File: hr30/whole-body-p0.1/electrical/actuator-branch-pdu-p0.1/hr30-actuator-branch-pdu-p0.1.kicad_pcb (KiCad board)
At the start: 6 copper layers, 82 x 42 mm, 78 parts, among them J1 12 V CONTROLLED INPUT, J101 CHANNEL 1 OUTPUT, J102 CHANNEL 2 OUTPUT, J103 CHANNEL 3 OUTPUT, J104 CHANNEL 4 OUTPUT, J105 CHANNEL 5 OUTPUT, J106 CHANNEL 6 OUTPUT, J2 6x DISABLE_OD + 6x PG, U201 TPS259474LRPWR circuit-breake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, U202 TPS259474LRPWR circuit-breake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, U203 TPS259474LRPWR circuit-breake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, U204 TPS259474LRPWR circuit-breake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, U205 TPS259474LRPWR circuit-breake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, U206 TPS259474LRPWR circuit-breake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

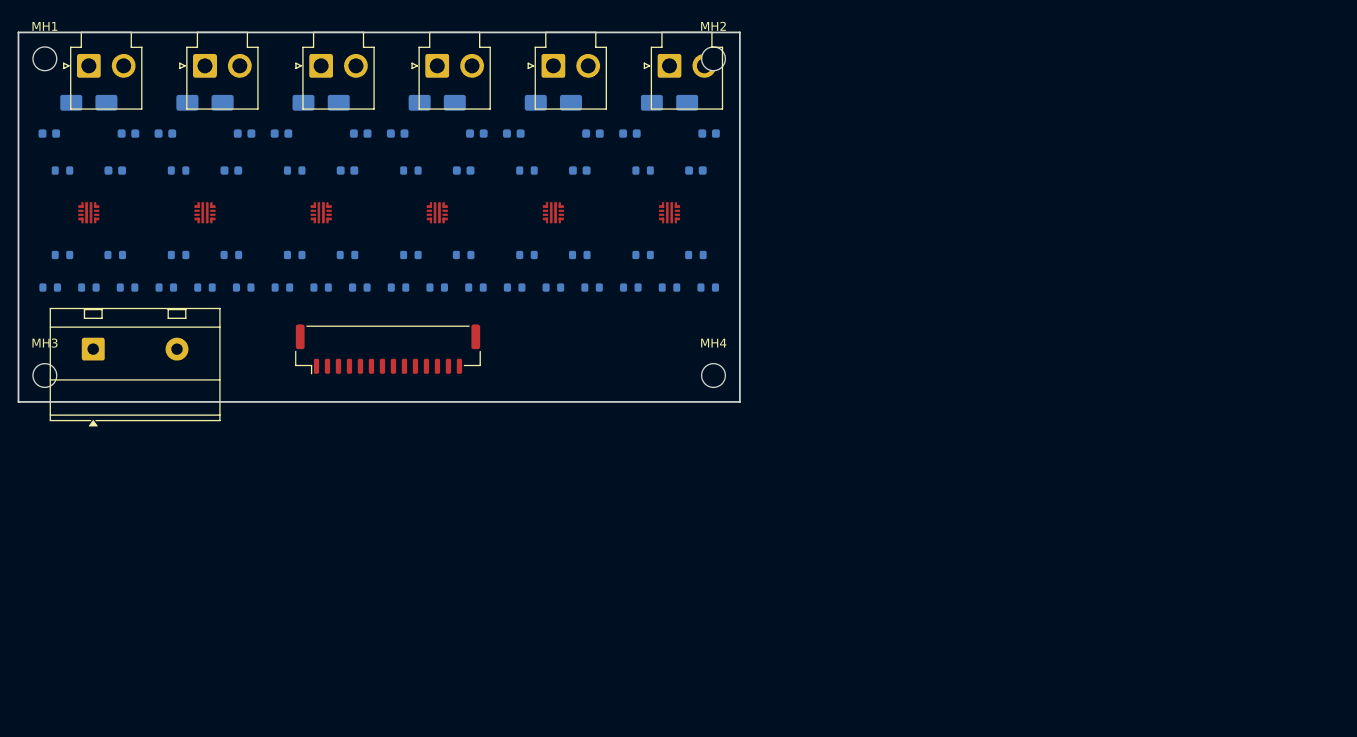
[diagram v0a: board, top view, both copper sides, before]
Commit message: Route HR-30 actuator branch PDU
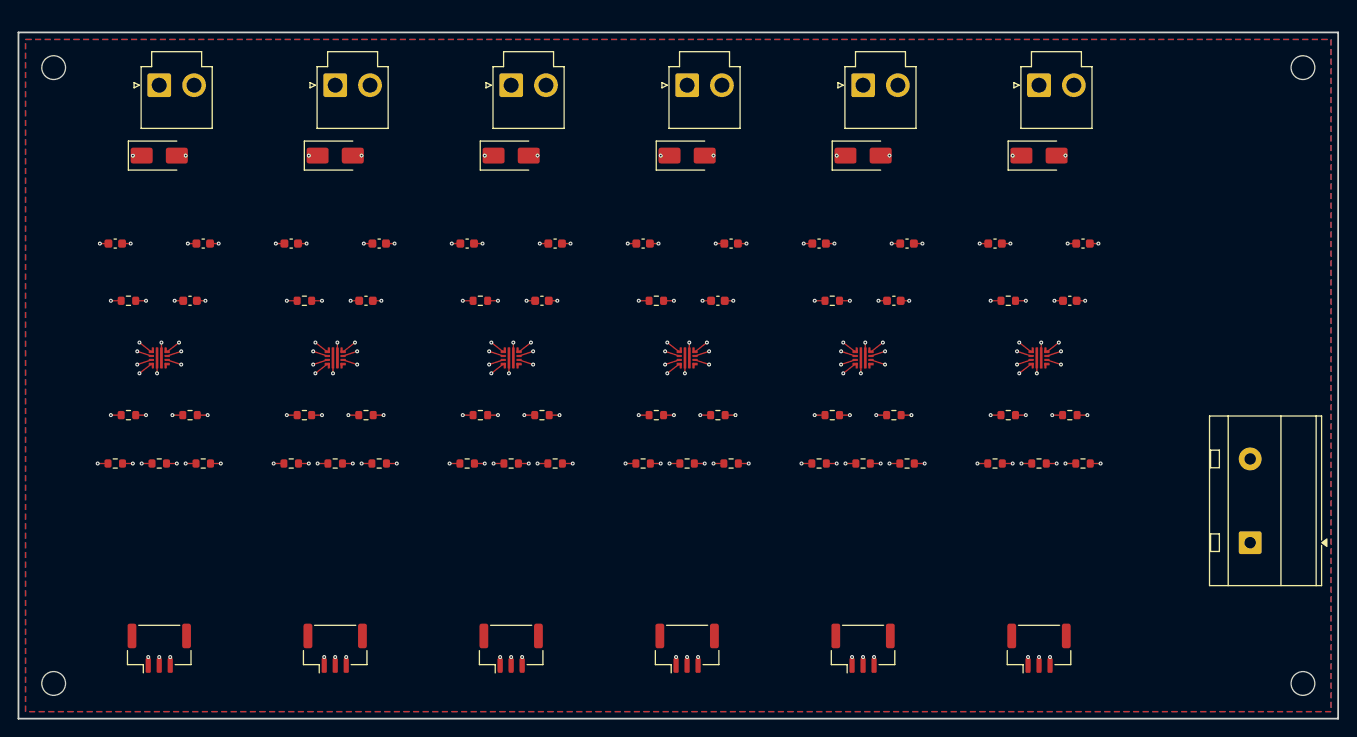
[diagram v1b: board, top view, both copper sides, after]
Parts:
- removed J2: 6x DISABLE_OD + 6x PG, JST_GH_BM14B-GHS-TBT_1x14-1MP_P1.25mm_Vertical
- added J201: CHANNEL 1 CONTROL, JST_GH_BM03B-GHS-TBT_1x03-1MP_P1.25mm_Vertical, F.Cu at (16.0, 70.0)
- added J202: CHANNEL 2 CONTROL, JST_GH_BM03B-GHS-TBT_1x03-1MP_P1.25mm_Vertical, F.Cu at (36.0, 70.0)
- added J203: CHANNEL 3 CONTROL, JST_GH_BM03B-GHS-TBT_1x03-1MP_P1.25mm_Vertical, F.Cu at (56.0, 70.0)
- added J204: CHANNEL 4 CONTROL, JST_GH_BM03B-GHS-TBT_1x03-1MP_P1.25mm_Vertical, F.Cu at (76.0, 70.0)
- added J205: CHANNEL 5 CONTROL, JST_GH_BM03B-GHS-TBT_1x03-1MP_P1.25mm_Vertical, F.Cu at (96.0, 70.0)
- added J206: CHANNEL 6 CONTROL, JST_GH_BM03B-GHS-TBT_1x03-1MP_P1.25mm_Vertical, F.Cu at (116.0, 70.0)
- C101, C102, C103, C201, C202, C203, C301, C302, C303, C401, C402, C403, C501, C502, C503, C601, C602, C603, D101, D201, D301, D401, D501, D601, R101, R102, R103, R104, R105, R106, R201, R202, R203, R204, R205, R206, R301, R302, R303, R304, R305, R306, R401, R402, R403, R404, R405, R406, R501, R502, R503, R504, R505, R506, R601, R602, R603, R604, R605, R606: moved to F.Cu
- moved J1 133.3 mm to (140.0, 58.0), turned to 90 degrees
- moved MH4 75.6 mm to (146.0, 74.0)
- moved MH2 67.0 mm to (146.0, 4.00)
- moved R603 47.1 mm to (121.0, 49.0), turned to 0 degrees
- moved R602 46.5 mm to (116.0, 49.0), turned to 0 degrees
- moved R605 46.2 mm to (119.5, 43.5), turned to 0 degrees
- moved R601 46.0 mm to (111.0, 49.0), turned to 0 degrees
- moved R604 45.3 mm to (112.5, 43.5), turned to 0 degrees
- moved U206 45.1 mm to (116.0, 37.0)
- moved C603 45.0 mm to (119.5, 30.5), turned to 0 degrees
- moved C602 44.3 mm to (121.0, 24.0), turned to 0 degrees
- moved R606 44.1 mm to (112.5, 30.5), turned to 0 degrees
- moved C601 43.3 mm to (111.0, 24.0), turned to 0 degrees
- moved D601 42.4 mm to (116.0, 14.0), turned to 0 degrees
- moved J106 42.1 mm to (116.0, 6.00)
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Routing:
- net PDU_12V_IN: track 0.00 -> 351.9 mm, vias 0 -> 18
- net PDU_0V: track 0.00 -> 60.5 mm, vias 0 -> 54
- net BRANCH_6_12V: track 0.00 -> 53.4 mm, vias 0 -> 4
- net BRANCH_5_12V: track 0.00 -> 53.4 mm, vias 0 -> 4
- net BRANCH_4_12V: track 0.00 -> 53.4 mm, vias 0 -> 4
- net BRANCH_3_12V: track 0.00 -> 53.4 mm, vias 0 -> 4
- net BRANCH_2_12V: track 0.00 -> 53.4 mm, vias 0 -> 4
- net BRANCH_1_12V: track 0.00 -> 53.4 mm, vias 0 -> 4
- net CH3_PG: track 0.00 -> 41.1 mm, vias 0 -> 2
- net CH2_PG: track 0.00 -> 41.1 mm, vias 0 -> 2
- net CH1_PG: track 0.00 -> 41.1 mm, vias 0 -> 2
- net CH6_PG: track 0.00 -> 41.1 mm, vias 0 -> 2
- net CH5_PG: track 0.00 -> 41.1 mm, vias 0 -> 2
- net CH4_PG: track 0.00 -> 41.1 mm, vias 0 -> 2
- net CH3_EN: track 0.00 -> 40.3 mm, vias 0 -> 4
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- added copper zone on B.Cu, net PDU_0V
- added copper zone on F.Cu, net PDU_0V
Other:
- board size 82 x 42 mm -> 150 x 78 mm
- copper layers 6 -> 10

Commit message: Install distributed HR-30 actuator power architecture
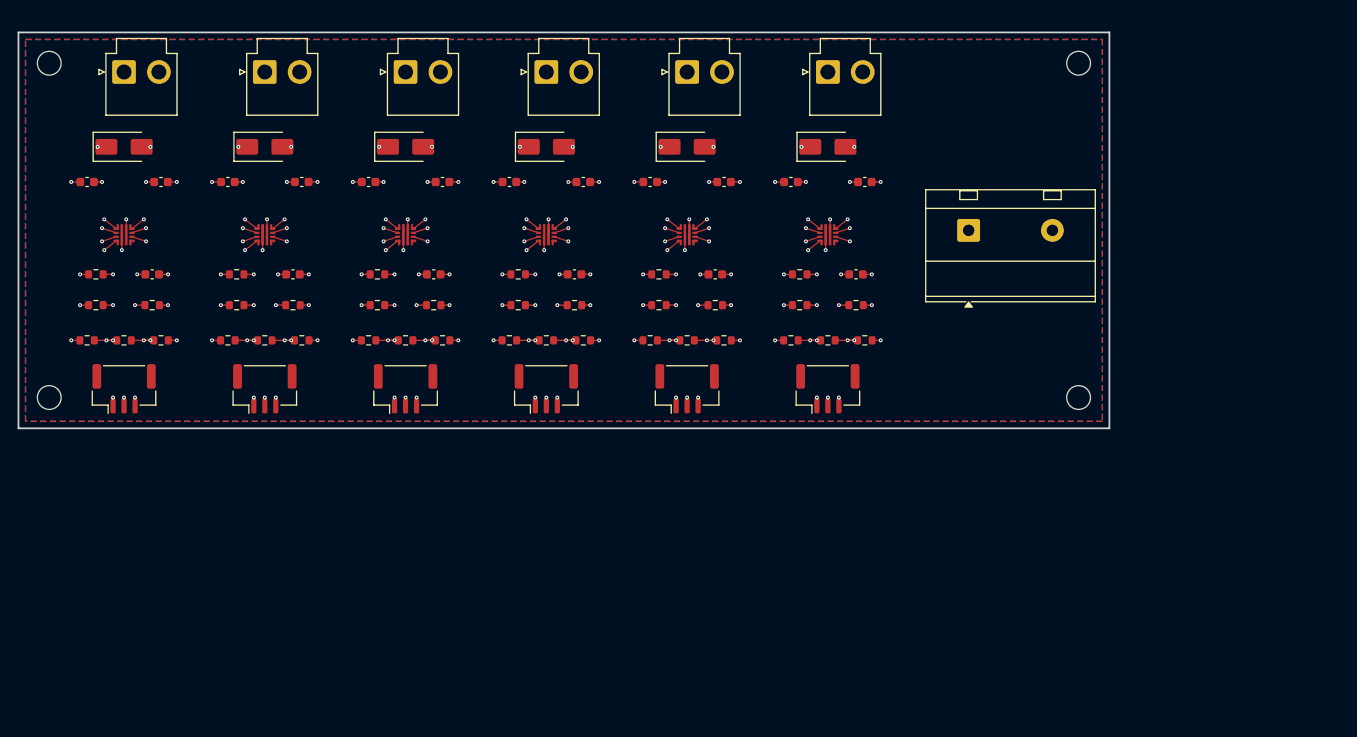
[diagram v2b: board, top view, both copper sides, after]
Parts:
- moved J1 47.8 mm to (108.0, 22.5), turned to 0 degrees
- moved MH4 41.3 mm to (120.5, 41.5)
- moved J206 38.0 mm to (92.0, 40.5)
- moved J205 35.6 mm to (76.0, 40.5)
- moved J204 33.6 mm to (60.0, 40.5)
- moved MH3 32.5 mm to (3.50, 41.5)
- moved J203 31.8 mm to (44.0, 40.5)
- moved J202 30.6 mm to (28.0, 40.5)
- moved J201 29.8 mm to (12.0, 40.5)
- moved R603 28.5 mm to (96.2, 35.0)
- moved R602 27.8 mm to (92.0, 35.0)
- moved U206 27.8 mm to (92.0, 23.0)
- moved R605 27.3 mm to (95.2, 31.0)
- moved R601 27.1 mm to (87.8, 35.0)
- moved R604 26.8 mm to (88.8, 31.0)
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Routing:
- net PDU_12V_IN: track 351.9 -> 289.5 mm
- net CH1_PG: track 41.1 -> 25.6 mm
- net CH6_PG: track 41.1 -> 25.6 mm
- net CH5_PG: track 41.1 -> 25.6 mm
- net CH3_PG: track 41.1 -> 25.6 mm
- net CH2_PG: track 41.1 -> 25.6 mm
- net CH4_PG: track 41.1 -> 25.6 mm
- net CH6_EN: track 40.3 -> 25.0 mm
- net CH5_EN: track 40.3 -> 25.0 mm
- net CH3_EN: track 40.3 -> 25.0 mm
- net CH1_EN: track 40.3 -> 25.0 mm
- net CH2_EN: track 40.3 -> 25.0 mm
- net CH4_EN: track 40.3 -> 25.0 mm
- net BRANCH_6_12V: track 53.4 -> 41.4 mm
- net BRANCH_5_12V: track 53.4 -> 41.4 mm
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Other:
- board size 150 x 78 mm -> 124 x 45 mm
- board text added: "COMMISSIONING ONLY"
- board text removed: "COMMISSIONING ONLY - REGEN / THERMAL OPEN"
